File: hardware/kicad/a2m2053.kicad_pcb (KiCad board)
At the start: 2 copper layers, 100 x 110 mm, 45 parts, among them J1 DB-19 female R/A (daisy chain), J2 CN104 mechanism, J3 CN102 host (FROM HOST), J4 Eject button, J5 In-use LED, U1 SN74LVC8T245DWR, U2 SN74LVC8T245DWR, U3 SN74LVC8T245DWR, U4 SN74LVC8T245DWR, U5 SN74LVC8T245DWR

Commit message: fix(pcb): tie the mechanism +5V group to the host +5V feed
J2.11/J2.20, C12 and the U5 feed were an island of the +5V pour, walled
off by the SEL/ENBL/WRTDATA drops and the +12V band. Add a 1.2 mm B.Cu
run at y 76.3 from the J2 strap to the x 151 host feed, stitch the two
small pour slivers near C12 and J2.11, drop the stray via. DRC with zone
refill: 0 errors, 0 unconnected.

Co-Authored-By: Claude Fable 5.1 <noreply@anthropic.com>
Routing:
- net +5V: track 138.2 -> 158.6 mm
- net /MECH_WRTGATE: vias 2 -> 1
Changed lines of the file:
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@@
+	)
+	(segment
+		(start 121.3 74.22)
+		(end 120.55 72.9)
+		(width 0.25)
+		(layer "F.Cu")
+		(net "+5V")
 	)
 	(segment
@@
 	)
 	(segment
+		(start 134.3 83.8)
+		(end 134.3 86)
+		(width 0.5)
+		(layer "F.Cu")
+		(net "+5V")
+	)
+	(segment
 		(start 125.25 86.8)
 		(end 125.25 89.5)
@@
 	)
 	(segment
+		(start 134.3 76.3)
+		(end 151 76.3)
+		(width 1.2)
+		(layer "B.Cu")
+		(net "+5V")
+	)
+	(segment
 		(start 133.5 71.68)
 		(end 133.5 76.3)
@@
 		(net "/MECH_WRTGATE")
 	)
-	(via
-		(at 120.03 72.95)
-		(size 0.6)
-		(drill 0.3)
-		(layers "F.Cu" "B.Cu")
-		(net "/MECH_WRTGATE")
-	)

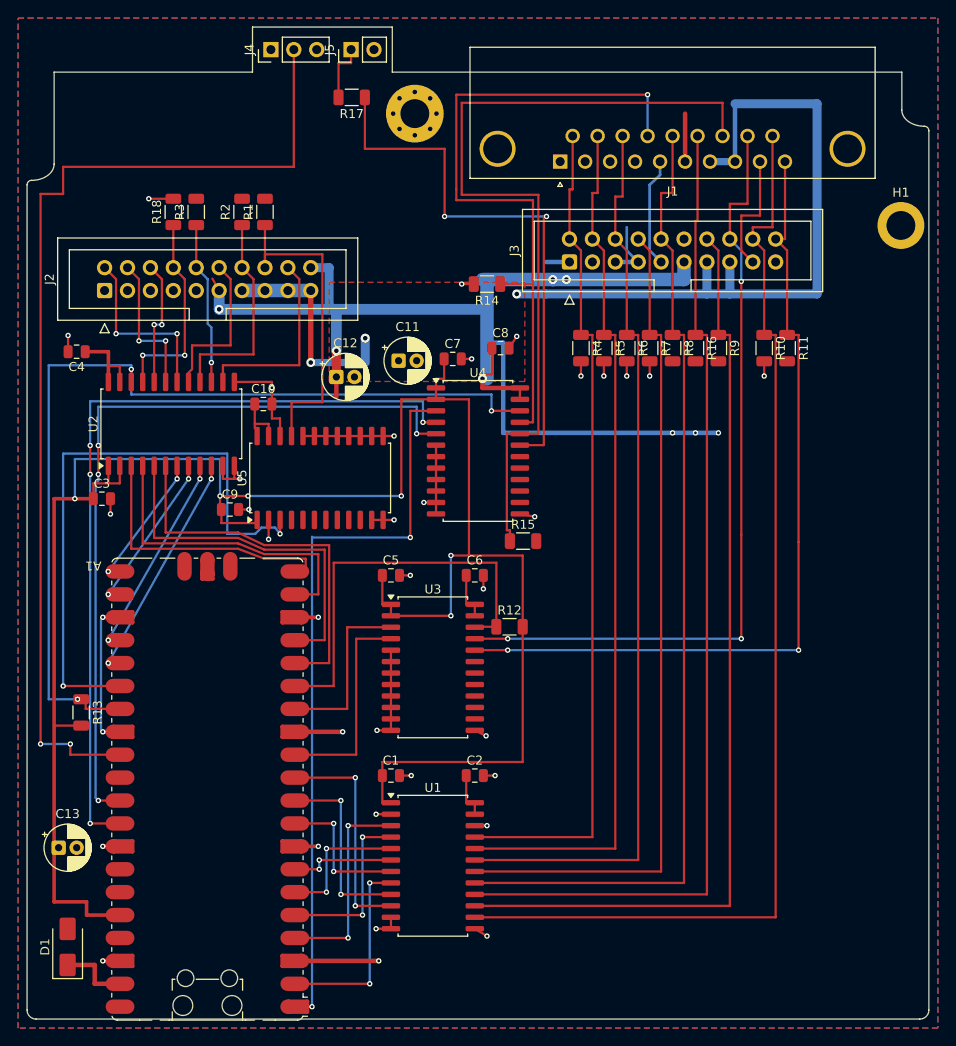
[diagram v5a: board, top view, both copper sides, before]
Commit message: experiment(pcb): Freerouting 2.5 clean-field result imported for comparison
All tracks and vias wiped, Freerouting routed every net from scratch
with no pours visible to it, session imported, zones refilled. 862
segments, 73 vias. Not DRC clean (import left 50 segments at 0.187 mm,
two ENBL_OUT pieces missing, GND traces on the board edge). Kept on this
branch for comparison only; main carries the hand-routed board.

Co-Authored-By: Claude Fable 5.1 <noreply@anthropic.com>
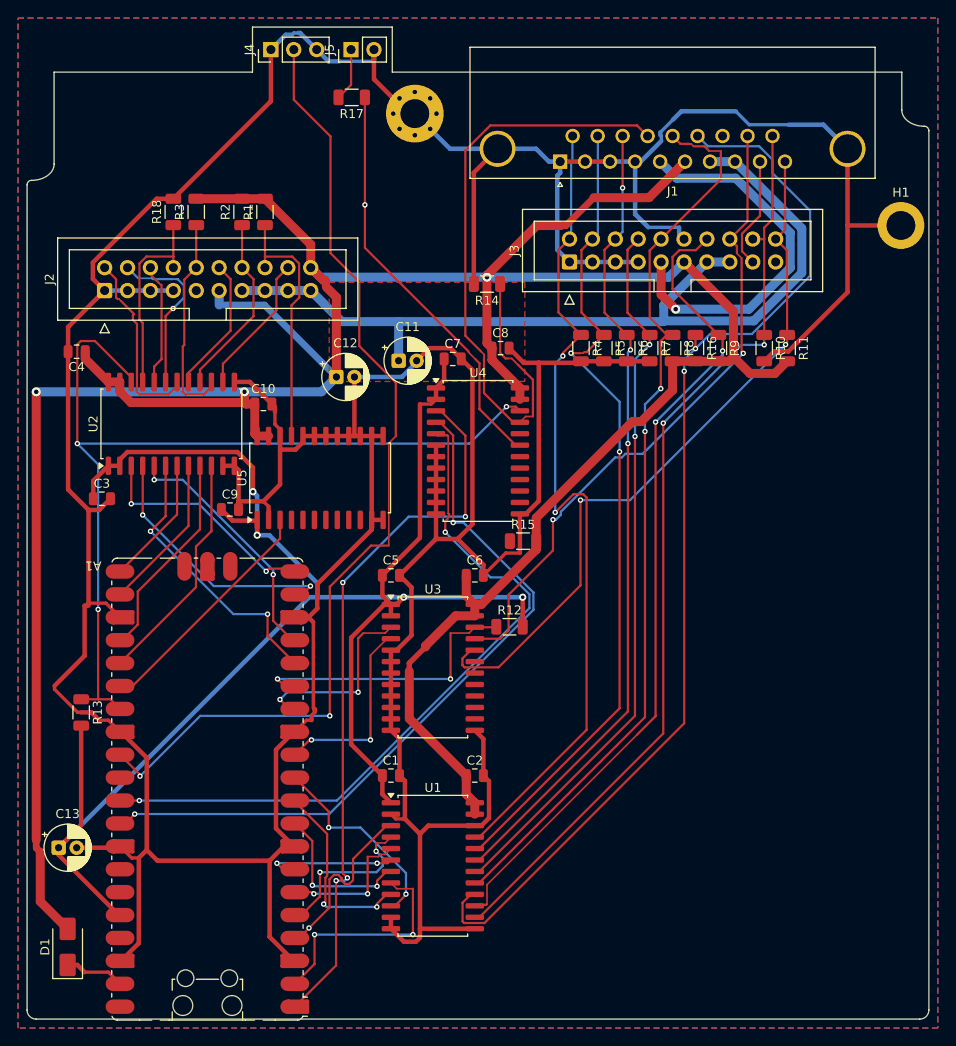
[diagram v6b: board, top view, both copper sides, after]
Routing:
- net GND: track 133.3 -> 626.7 mm, vias 37 -> 0
- net +5V: track 158.6 -> 355.2 mm, vias 8 -> 3
- net /ENBL_OUT: track 92.5 -> 0.00 mm
- net /MECH_RD_A: track 66.2 -> 26.6 mm, vias 2 -> 0
- net +3V3: track 230.5 -> 197.7 mm, vias 6 -> 4
- net -12V: track 12.2 -> 42.1 mm, vias 0 -> 1
- net /HOST_WR: track 124.0 -> 103.3 mm, vias 0 -> 2
- net /LED_B: track 61.6 -> 46.0 mm, vias 2 -> 1
- net /HOST_RD: track 87.8 -> 72.9 mm, vias 3 -> 2
- net /U3_OE: track 45.5 -> 31.9 mm, vias 0 -> 2
- net /HOST_HSTEN: track 104.0 -> 90.9 mm, vias 0 -> 2
- net /HOST_ACK: track 92.9 -> 80.1 mm
- net /HOST_PH3: track 92.6 -> 80.0 mm, vias 0 -> 2
- net /CA1_A: track 39.5 -> 27.8 mm, vias 0 -> 2
- net /HOST_PH2: track 101.0 -> 89.8 mm, vias 0 -> 3
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
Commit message: experiment(pcb): Freerouting result hand-fixed to DRC clean
Narrow neck-down segments widened, ENBL_OUT completed, GND traces
pulled off the board edge, a few vias dragged. DRC with zone refill:
0 errors, 0 unconnected. +5V, +12V and GND each verify as one
connectivity cluster. 870 segments, 81 vias.

Co-Authored-By: Claude Fable 5.1 <noreply@anthropic.com>
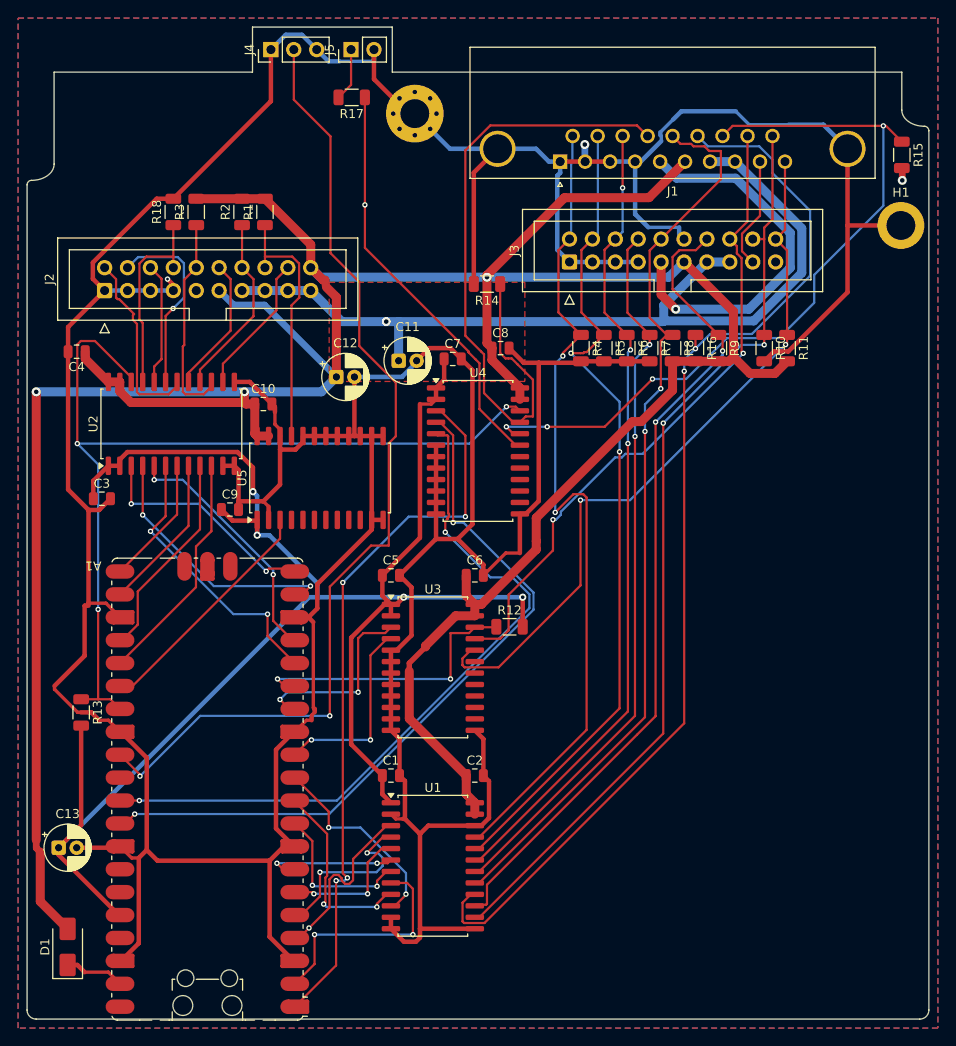
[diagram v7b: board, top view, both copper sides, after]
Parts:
- moved R15 60.0 mm to (197.0, 59.2), turned to -90 degrees
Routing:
- net /ENBL_OUT: track 0.00 -> 85.5 mm, vias 0 -> 4
- net GND: track 626.7 -> 629.9 mm, vias 0 -> 2
- net /MECH_CA1: track 18.6 -> 21.0 mm
- net /PH1_A: track 18.3 -> 19.8 mm
- net +5V: track 355.2 -> 355.7 mm, vias 3 -> 4
- net +12V: vias 0 -> 1

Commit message: feat(pcb): Byte Hamr logo and board text, FG merged into GND
Silkscreen: logo_sm footprint from Byte Hamr rev 2 (copied into the
project library), title, revision and ID block in the bottom-right
corner. Board named Disk Hamr.

Schematic: the three FG global labels on H1, H2 and the J1 shield become
GND power symbols; FG was a fit-test placeholder, frame ground is the
same return. PCB pads were already on GND. Schematic parity, DRC with
refill and ERC are clean apart from the pre-existing Pico AGND/GND pin
type error.

Co-Authored-By: Claude Fable 5.1 <noreply@anthropic.com>
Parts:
- added G1: logo_sm, a2m2053:logo_sm, F.Cu at (187.2, 146.2)
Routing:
- net GND: track 629.9 -> 653.2 mm, vias 2 -> 7
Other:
- board text added: "DH-1-0 4226 Robert Rico"
- board text added: "Disk Hamr"
- board text added: "Rev. 1.0"
